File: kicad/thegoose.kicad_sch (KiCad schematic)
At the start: 0 parts

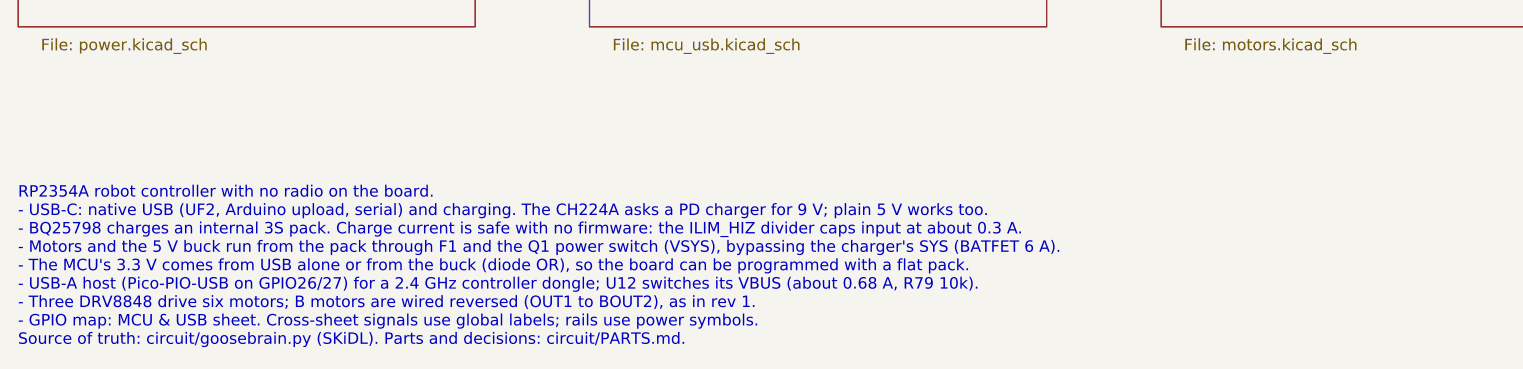
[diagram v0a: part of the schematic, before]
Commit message: Rotate U10 to 0 deg and re-place the brain at 66.6 x 32 mm, unrouted
USB now runs straight down from J1 into U10's north pins; IO goes west to J5,
which moves to the top of the left wall with M5/M6 below it. SW1 sits under
U16 and SW2 in the bottom-right corner; Q1 is east of J3. GPIO map redone for
the new orientation (IO1-6 on GPIO0-3/8/9, motors on GPIO12-17/20-23/26-27,
USB-A on GPIO24/25, LED on GPIO29). ERC clean, DRC parity clean.

Co-Authored-By: Claude Opus 5.5 <noreply@anthropic.com>
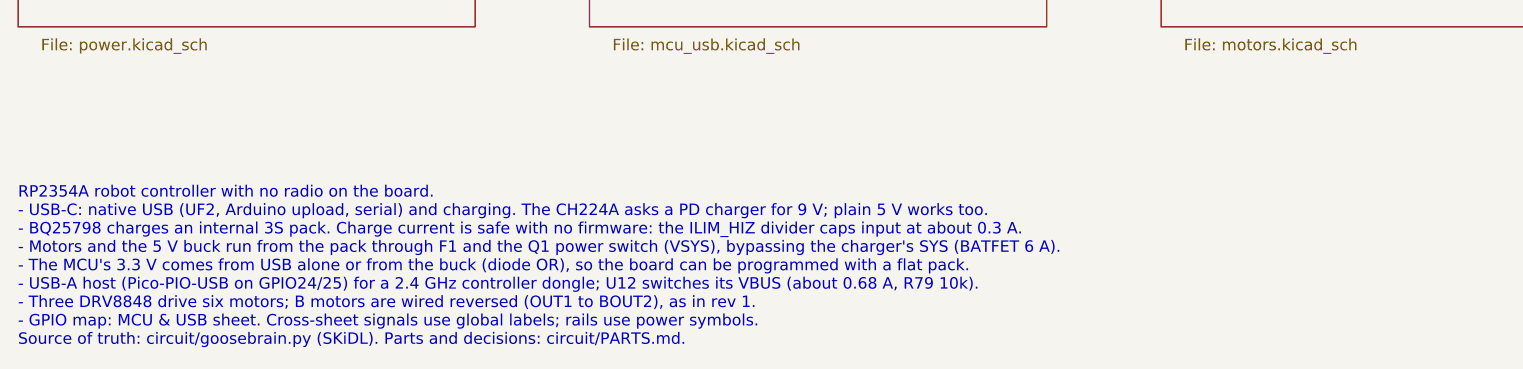
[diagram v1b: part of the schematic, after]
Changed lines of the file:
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@@
 		)
 	)
-	(text "RP2354A robot controller with no radio on the board.\n- USB-C: native USB (UF2, Arduino upload, serial) and charging. The CH224A asks a PD charger for 9 V; plain 5 V works too.\n- BQ25798 charges an internal 3S pack. Charge current is safe with no firmware: the ILIM_HIZ divider caps input at about 0.3 A.\n- Motors and the 5 V buck run from the pack through F1 and the Q1 power switch (VSYS), bypassing the charger's SYS (BATFET 6 A).\n- The MCU's 3.3 V comes from USB alone or from the buck (diode OR), so the board can be programmed with a flat pack.\n- USB-A host (Pico-PIO-USB on GPIO26/27) for a 2.4 GHz controller dongle; U12 switches its VBUS (about 0.68 A, R79 10k).\n- Three DRV8848 drive six motors; B motors are wired reversed (OUT1 to BOUT2), as in rev 1.\n- GPIO map: MCU & USB sheet. Cross-sheet signals use global labels; rails use power symbols.\nSource of truth: circuit/goosebrain.py (SKiDL). Parts and decisions: circuit/PARTS.md."
+	(text "RP2354A robot controller with no radio on the board.\n- USB-C: native USB (UF2, Arduino upload, serial) and charging. The CH224A asks a PD charger for 9 V; plain 5 V works too.\n- BQ25798 charges an internal 3S pack. Charge current is safe with no firmware: the ILIM_HIZ divider caps input at about 0.3 A.\n- Motors and the 5 V buck run from the pack through F1 and the Q1 power switch (VSYS), bypassing the charger's SYS (BATFET 6 A).\n- The MCU's 3.3 V comes from USB alone or from the buck (diode OR), so the board can be programmed with a flat pack.\n- USB-A host (Pico-PIO-USB on GPIO24/25) for a 2.4 GHz controller dongle; U12 switches its VBUS (about 0.68 A, R79 10k).\n- Three DRV8848 drive six motors; B motors are wired reversed (OUT1 to BOUT2), as in rev 1.\n- GPIO map: MCU & USB sheet. Cross-sheet signals use global labels; rails use power symbols.\nSource of truth: circuit/goosebrain.py (SKiDL). Parts and decisions: circuit/PARTS.md."
 		(exclude_from_sim no)
 		(at 25.4 81.28 0)
